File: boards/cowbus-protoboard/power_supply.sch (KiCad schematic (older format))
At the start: 3 parts

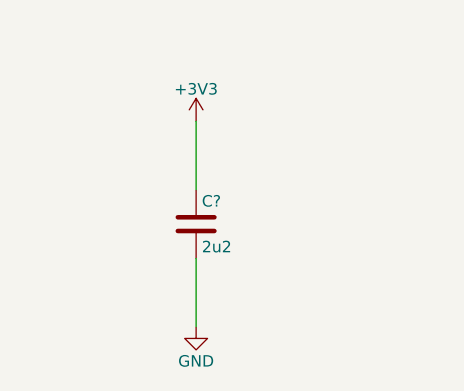
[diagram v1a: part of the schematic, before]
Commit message: values added, 100n for uC added
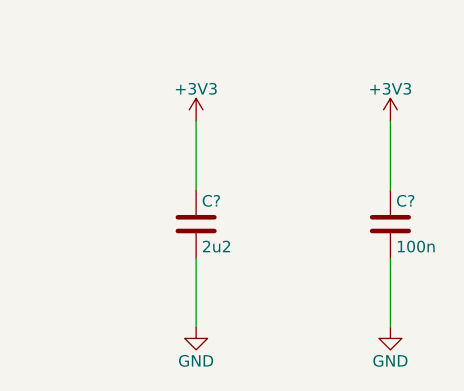
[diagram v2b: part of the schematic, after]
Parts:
- added C?: 100n, symbol C
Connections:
- net +3V3: now also C?.1
- net GND: now also C?.2
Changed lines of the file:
@@
 encoding utf-8
 Sheet 3 6
-Title ""
-Date ""
-Rev ""
+Title "cowbus protoboard"
+Date "2015-07-15"
+Rev "0.9"
 Comp ""
 Comment1 ""
@@
 Wire Wire Line
 	4450 3450 4450 4000
+$Comp
+L GND #PWR?
+U 1 1 55A95D68
+P 8250 4600
+F 0 "#PWR?" H 8250 4350 50  0001 C CNN
+F 1 "GND" H 8250 4450 50  0000 C CNN
+F 2 "" H 8250 4600 60  0000 C CNN
+F 3 "" H 8250 4600 60  0000 C CNN
+	1    8250 4600
+	1    0    0    -1
+$EndComp
+$Comp
+L +3V3 #PWR?
+U 1 1 55A95D6E
+P 8250 3700
+F 0 "#PWR?" H 8250 3550 50  0001 C CNN
+F 1 "+3V3" H 8250 3840 50  0000 C CNN
+F 2 "" H 8250 3700 60  0000 C CNN
+F 3 "" H 8250 3700 60  0000 C CNN
+	1    8250 3700
+	1    0    0    -1
+$EndComp
+$Comp
+L C C?
+U 1 1 55A95D76
+P 8250 4150
+F 0 "C?" H 8275 4250 50  0000 L CNN
+F 1 "100n" H 8275 4050 50  0000 L CNN
+F 2 "" H 8288 4000 30  0000 C CNN
+F 3 "" H 8250 4150 60  0000 C CNN
+	1    8250 4150
+	1    0    0    -1
+$EndComp
+Wire Wire Line
+	8250 4000 8250 3700
+Wire Wire Line
+	8250 4600 8250 4300
 $EndSCHEMATC

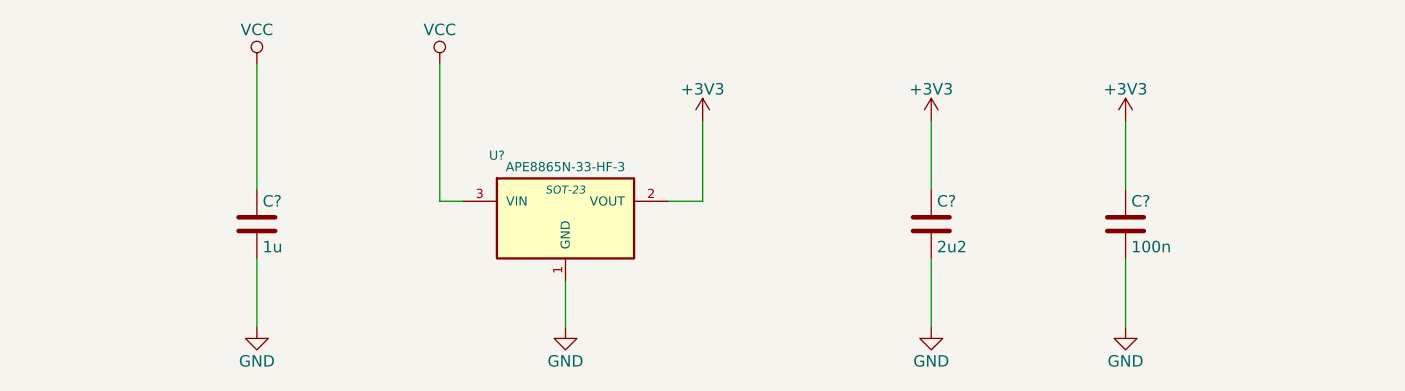
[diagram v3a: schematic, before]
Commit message: some footprint assignments done
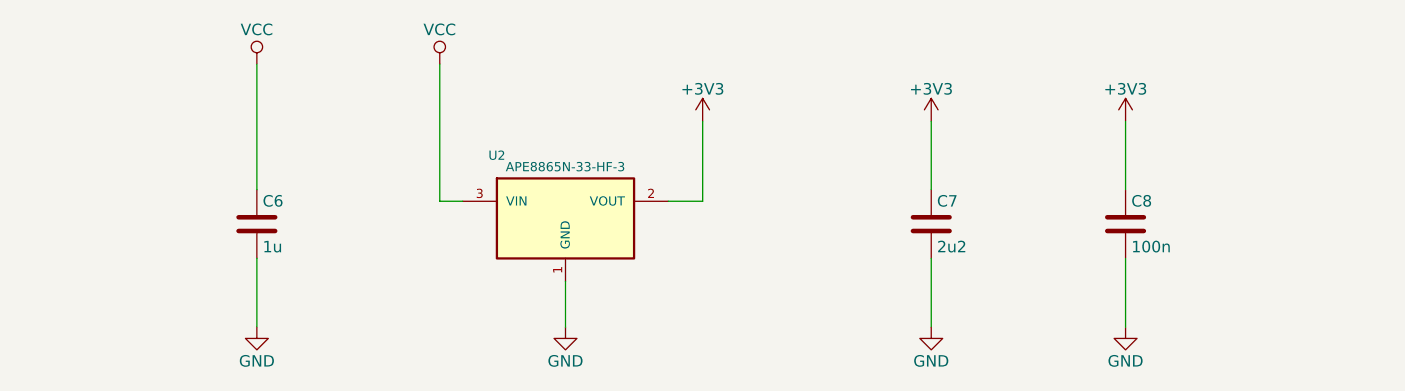
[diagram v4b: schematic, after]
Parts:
- C6, C7, C8: renamed from C?; footprint (none) -> Capacitors_SMD:C_0805_HandSoldering
- U2: renamed from U?; footprint SOT-23 -> (none)
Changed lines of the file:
@@
 $EndDescr
 $Comp
-L APE8865N-33-HF-3 U?
+L APE8865N-33-HF-3 U2
 U 1 1 55A5144A
 P 5800 4100
-F 0 "U?" H 5500 4350 40  0000 C CNN
+F 0 "U2" H 5500 4350 40  0000 C CNN
 F 1 "APE8865N-33-HF-3" H 5800 4300 40  0000 C CNN
-F 2 "SOT-23" H 5800 4200 35  0000 C CIN
+F 2 "" H 5800 4200 35  0001 C CIN
 F 3 "" H 5800 4100 60  0000 C CNN
 	1    5800 4100
@@
 $EndComp
 $Comp
-L C C?
+L C C6
 U 1 1 55A51451
 P 4450 4150
-F 0 "C?" H 4475 4250 50  0000 L CNN
+F 0 "C6" H 4475 4250 50  0000 L CNN
 F 1 "1u" H 4475 4050 50  0000 L CNN
-F 2 "" H 4488 4000 30  0000 C CNN
+F 2 "Capacitors_SMD:C_0805_HandSoldering" H 4488 4000 30  0001 C CNN
 F 3 "" H 4450 4150 60  0000 C CNN
 	1    4450 4150
@@
 $EndComp
 $Comp
-L C C?
+L C C7
 U 1 1 55A51458
 P 7400 4150
-F 0 "C?" H 7425 4250 50  0000 L CNN
+F 0 "C7" H 7425 4250 50  0000 L CNN
 F 1 "2u2" H 7425 4050 50  0000 L CNN
-F 2 "" H 7438 4000 30  0000 C CNN
+F 2 "Capacitors_SMD:C_0805_HandSoldering" H 7438 4000 30  0001 C CNN
 F 3 "" H 7400 4150 60  0000 C CNN
 	1    7400 4150
@@
 $EndComp
 $Comp
-L VCC #PWR?
+L VCC #PWR022
 U 1 1 55A515B6
 P 5250 3450
-F 0 "#PWR?" H 5250 3300 50  0001 C CNN
+F 0 "#PWR022" H 5250 3300 50  0001 C CNN
 F 1 "VCC" H 5250 3600 50  0000 C CNN
 F 2 "" H 5250 3450 60  0000 C CNN
@@
 	5250 3450 5250 4050
 $Comp
-L +3V3 #PWR?
+L +3V3 #PWR023
 U 1 1 55A515EF
 P 6400 3700
-F 0 "#PWR?" H 6400 3550 50  0001 C CNN
+F 0 "#PWR023" H 6400 3550 50  0001 C CNN
 F 1 "+3V3" H 6400 3840 50  0000 C CNN
 F 2 "" H 6400 3700 60  0000 C CNN
@@
 	6400 4050 6400 3700
 $Comp
-L GND #PWR?
+L GND #PWR024
 U 1 1 55A51658
 P 5800 4600
-F 0 "#PWR?" H 5800 4350 50  0001 C CNN
+F 0 "#PWR024" H 5800 4350 50  0001 C CNN
 F 1 "GND" H 5800 4450 50  0000 C CNN
 F 2 "" H 5800 4600 60  0000 C CNN
@@
 	5800 4600 5800 4400
 $Comp
-L VCC #PWR?
+L VCC #PWR025
 U 1 1 55A5185F
 P 4450 3450
-F 0 "#PWR?" H 4450 3300 50  0001 C CNN
+F 0 "#PWR025" H 4450 3300 50  0001 C CNN
 F 1 "VCC" H 4450 3600 50  0000 C CNN
 F 2 "" H 4450 3450 60  0000 C CNN
@@
 $EndComp
 $Comp
-L GND #PWR?
+L GND #PWR026
 U 1 1 55A51873
 P 4450 4600
-F 0 "#PWR?" H 4450 4350 50  0001 C CNN
+F 0 "#PWR026" H 4450 4350 50  0001 C CNN
 F 1 "GND" H 4450 4450 50  0000 C CNN
 F 2 "" H 4450 4600 60  0000 C CNN
@@
 $EndComp
 $Comp
-L GND #PWR?
+L GND #PWR027
 U 1 1 55A51887
 P 7400 4600
-F 0 "#PWR?" H 7400 4350 50  0001 C CNN
+F 0 "#PWR027" H 7400 4350 50  0001 C CNN
 F 1 "GND" H 7400 4450 50  0000 C CNN
 F 2 "" H 7400 4600 60  0000 C CNN
@@
 $EndComp
 $Comp
-L +3V3 #PWR?
+L +3V3 #PWR028
 U 1 1 55A518AE
 P 7400 3700
-F 0 "#PWR?" H 7400 3550 50  0001 C CNN
+F 0 "#PWR028" H 7400 3550 50  0001 C CNN
 F 1 "+3V3" H 7400 3840 50  0000 C CNN
 F 2 "" H 7400 3700 60  0000 C CNN
@@
 	4450 3450 4450 4000
 $Comp
-L GND #PWR?
+L GND #PWR029
 U 1 1 55A95D68
 P 8250 4600
-F 0 "#PWR?" H 8250 4350 50  0001 C CNN
+F 0 "#PWR029" H 8250 4350 50  0001 C CNN
 F 1 "GND" H 8250 4450 50  0000 C CNN
 F 2 "" H 8250 4600 60  0000 C CNN
@@
 $EndComp
 $Comp
-L +3V3 #PWR?
+L +3V3 #PWR030
 U 1 1 55A95D6E
 P 8250 3700
-F 0 "#PWR?" H 8250 3550 50  0001 C CNN
+F 0 "#PWR030" H 8250 3550 50  0001 C CNN
 F 1 "+3V3" H 8250 3840 50  0000 C CNN
 F 2 "" H 8250 3700 60  0000 C CNN
@@
 $EndComp
 $Comp
-L C C?
+L C C8
 U 1 1 55A95D76
 P 8250 4150
-F 0 "C?" H 8275 4250 50  0000 L CNN
+F 0 "C8" H 8275 4250 50  0000 L CNN
 F 1 "100n" H 8275 4050 50  0000 L CNN
-F 2 "" H 8288 4000 30  0000 C CNN
+F 2 "Capacitors_SMD:C_0805_HandSoldering" H 8288 4000 30  0001 C CNN
 F 3 "" H 8250 4150 60  0000 C CNN
 	1    8250 4150

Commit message: first version of layout for protoboard
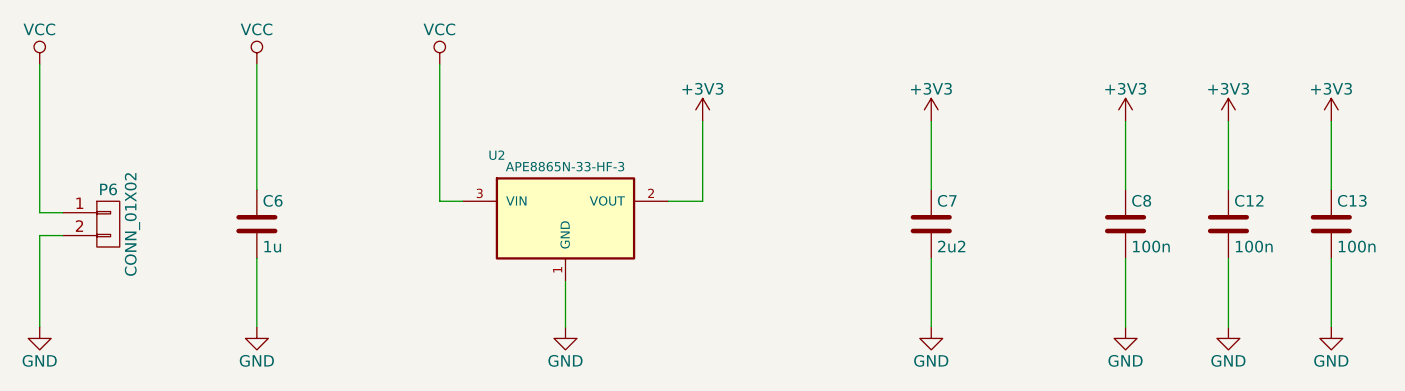
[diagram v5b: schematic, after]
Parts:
- added C12, C13: 100n, Capacitors_SMD:C_0805_HandSoldering, symbol C
- added P6: CONN_01X02, Pin_Headers:Pin_Header_Straight_1x02, symbol CONN_01X02
- U2: footprint (none) -> Housings_SOT-23_SOT-143_TSOT-6:SOT-23_Handsoldering
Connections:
- net +3V3: now also C12.1, C13.1
- net GND: now also C12.2, C13.2, P6.2 (P2)
- net VCC: now also P6.1 (P1)
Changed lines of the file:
@@
 EESchema Schematic File Version 2
+LIBS:cowbus-protoboard-rescue
 LIBS:power
 LIBS:device
@@
 LIBS:nrf24l01plus-module
 LIBS:i2c
+LIBS:led_rgb_reichelt
 LIBS:cowbus-protoboard-cache
 EELAYER 25 0
@@
 F 0 "U2" H 5500 4350 40  0000 C CNN
 F 1 "APE8865N-33-HF-3" H 5800 4300 40  0000 C CNN
-F 2 "" H 5800 4200 35  0001 C CIN
+F 2 "Housings_SOT-23_SOT-143_TSOT-6:SOT-23_Handsoldering" H 5800 4200 35  0001 C CIN
 F 3 "" H 5800 4100 60  0000 C CNN
 	1    5800 4100
@@
 $EndComp
 $Comp
-L VCC #PWR022
+L VCC #PWR27
 U 1 1 55A515B6
 P 5250 3450
-F 0 "#PWR022" H 5250 3300 50  0001 C CNN
+F 0 "#PWR27" H 5250 3300 50  0001 C CNN
 F 1 "VCC" H 5250 3600 50  0000 C CNN
 F 2 "" H 5250 3450 60  0000 C CNN
@@
 	5250 3450 5250 4050
 $Comp
-L +3V3 #PWR023
+L +3V3 #PWR29
 U 1 1 55A515EF
 P 6400 3700
-F 0 "#PWR023" H 6400 3550 50  0001 C CNN
+F 0 "#PWR29" H 6400 3550 50  0001 C CNN
 F 1 "+3V3" H 6400 3840 50  0000 C CNN
 F 2 "" H 6400 3700 60  0000 C CNN
@@
 	6400 4050 6400 3700
 $Comp
-L GND #PWR024
+L GND #PWR28
 U 1 1 55A51658
 P 5800 4600
-F 0 "#PWR024" H 5800 4350 50  0001 C CNN
+F 0 "#PWR28" H 5800 4350 50  0001 C CNN
 F 1 "GND" H 5800 4450 50  0000 C CNN
 F 2 "" H 5800 4600 60  0000 C CNN
@@
 	5800 4600 5800 4400
 $Comp
-L VCC #PWR025
+L VCC #PWR25
 U 1 1 55A5185F
 P 4450 3450
-F 0 "#PWR025" H 4450 3300 50  0001 C CNN
+F 0 "#PWR25" H 4450 3300 50  0001 C CNN
 F 1 "VCC" H 4450 3600 50  0000 C CNN
 F 2 "" H 4450 3450 60  0000 C CNN
@@
 $EndComp
 $Comp
-L GND #PWR026
+L GND #PWR26
 U 1 1 55A51873
 P 4450 4600
-F 0 "#PWR026" H 4450 4350 50  0001 C CNN
+F 0 "#PWR26" H 4450 4350 50  0001 C CNN
 F 1 "GND" H 4450 4450 50  0000 C CNN
 F 2 "" H 4450 4600 60  0000 C CNN
@@
 $EndComp
 $Comp
-L GND #PWR027
+L GND #PWR31
 U 1 1 55A51887
 P 7400 4600
-F 0 "#PWR027" H 7400 4350 50  0001 C CNN
+F 0 "#PWR31" H 7400 4350 50  0001 C CNN
 F 1 "GND" H 7400 4450 50  0000 C CNN
 F 2 "" H 7400 4600 60  0000 C CNN
@@
 $EndComp
 $Comp
-L +3V3 #PWR028
+L +3V3 #PWR30
 U 1 1 55A518AE
 P 7400 3700
-F 0 "#PWR028" H 7400 3550 50  0001 C CNN
+F 0 "#PWR30" H 7400 3550 50  0001 C CNN
 F 1 "+3V3" H 7400 3840 50  0000 C CNN
 F 2 "" H 7400 3700 60  0000 C CNN
@@
 	4450 3450 4450 4000
 $Comp
-L GND #PWR029
+L GND #PWR33
 U 1 1 55A95D68
 P 8250 4600
-F 0 "#PWR029" H 8250 4350 50  0001 C CNN
+F 0 "#PWR33" H 8250 4350 50  0001 C CNN
 F 1 "GND" H 8250 4450 50  0000 C CNN
 F 2 "" H 8250 4600 60  0000 C CNN
@@
 $EndComp
 $Comp
-L +3V3 #PWR030
+L +3V3 #PWR32
 U 1 1 55A95D6E
 P 8250 3700
-F 0 "#PWR030" H 8250 3550 50  0001 C CNN
+F 0 "#PWR32" H 8250 3550 50  0001 C CNN
 F 1 "+3V3" H 8250 3840 50  0000 C CNN
 F 2 "" H 8250 3700 60  0000 C CNN
@@
 Wire Wire Line
 	8250 4600 8250 4300
+$Comp
+L CONN_01X02 P6
+U 1 1 55BA81F9
+P 3800 4150
+F 0 "P6" H 3800 4300 50  0000 C CNN
+F 1 "CONN_01X02" V 3900 4150 50  0000 C CNN
+F 2 "Pin_Headers:Pin_Header_Straight_1x02" H 3800 4150 60  0001 C CNN
+F 3 "" H 3800 4150 60  0000 C CNN
+	1    3800 4150
+	1    0    0    -1
+$EndComp
+$Comp
+L VCC #PWR23
+U 1 1 55BA82A3
+P 3500 3450
+F 0 "#PWR23" H 3500 3300 50  0001 C CNN
+F 1 "VCC" H 3500 3600 50  0000 C CNN
+F 2 "" H 3500 3450 60  0000 C CNN
+F 3 "" H 3500 3450 60  0000 C CNN
+	1    3500 3450
+	1    0    0    -1
+$EndComp
+Wire Wire Line
+	3500 3450 3500 4100
+$Comp
+L GND #PWR24
+U 1 1 55BA82C3
+P 3500 4600
+F 0 "#PWR24" H 3500 4350 50  0001 C CNN
+F 1 "GND" H 3500 4450 50  0000 C CNN
+F 2 "" H 3500 4600 60  0000 C CNN
+F 3 "" H 3500 4600 60  0000 C CNN
+	1    3500 4600
+	1    0    0    -1
+$EndComp
+Wire Wire Line
+	3500 4200 3500 4600
+Wire Wire Line
+	3600 4200 3500 4200
+Wire Wire Line
+	3500 4100 3600 4100
+$Comp
+L GND #PWR35
+U 1 1 55BBC2D8
+P 8700 4600
+F 0 "#PWR35" H 8700 4350 50  0001 C CNN
+F 1 "GND" H 8700 4450 50  0000 C CNN
+F 2 "" H 8700 4600 60  0000 C CNN
+F 3 "" H 8700 4600 60  0000 C CNN
+	1    8700 4600
+	1    0    0    -1
+$EndComp
+$Comp
+L +3V3 #PWR34
+U 1 1 55BBC2DE
+P 8700 3700
+F 0 "#PWR34" H 8700 3550 50  0001 C CNN
+F 1 "+3V3" H 8700 3840 50  0000 C CNN
+F 2 "" H 8700 3700 60  0000 C CNN
+F 3 "" H 8700 3700 60  0000 C CNN
+	1    8700 3700
+	1    0    0    -1
+$EndComp
+$Comp
+L C C12
+U 1 1 55BBC2E4
+P 8700 4150
+F 0 "C12" H 8725 4250 50  0000 L CNN
+F 1 "100n" H 8725 4050 50  0000 L CNN
+F 2 "Capacitors_SMD:C_0805_HandSoldering" H 8738 4000 30  0001 C CNN
+F 3 "" H 8700 4150 60  0000 C CNN
+	1    8700 4150
+	1    0    0    -1
+$EndComp
+Wire Wire Line
+	8700 4000 8700 3700
+Wire Wire Line
+	8700 4600 8700 4300
+$Comp
+L GND #PWR37
+U 1 1 55BBC31A
+P 9150 4600
+F 0 "#PWR37" H 9150 4350 50  0001 C CNN
+F 1 "GND" H 9150 4450 50  0000 C CNN
+F 2 "" H 9150 4600 60  0000 C CNN
+F 3 "" H 9150 4600 60  0000 C CNN
+	1    9150 4600
+	1    0    0    -1
+$EndComp
+$Comp
+L +3V3 #PWR36
+U 1 1 55BBC320
+P 9150 3700
+F 0 "#PWR36" H 9150 3550 50  0001 C CNN
+F 1 "+3V3" H 9150 3840 50  0000 C CNN
+F 2 "" H 9150 3700 60  0000 C CNN
+F 3 "" H 9150 3700 60  0000 C CNN
+	1    9150 3700
+	1    0    0    -1
+$EndComp
+$Comp
+L C C13
+U 1 1 55BBC326
+P 9150 4150
+F 0 "C13" H 9175 4250 50  0000 L CNN
+F 1 "100n" H 9175 4050 50  0000 L CNN
+F 2 "Capacitors_SMD:C_0805_HandSoldering" H 9188 4000 30  0001 C CNN
+F 3 "" H 9150 4150 60  0000 C CNN
+	1    9150 4150
+	1    0    0    -1
+$EndComp
+Wire Wire Line
+	9150 4000 9150 3700
+Wire Wire Line
+	9150 4600 9150 4300
 $EndSCHEMATC

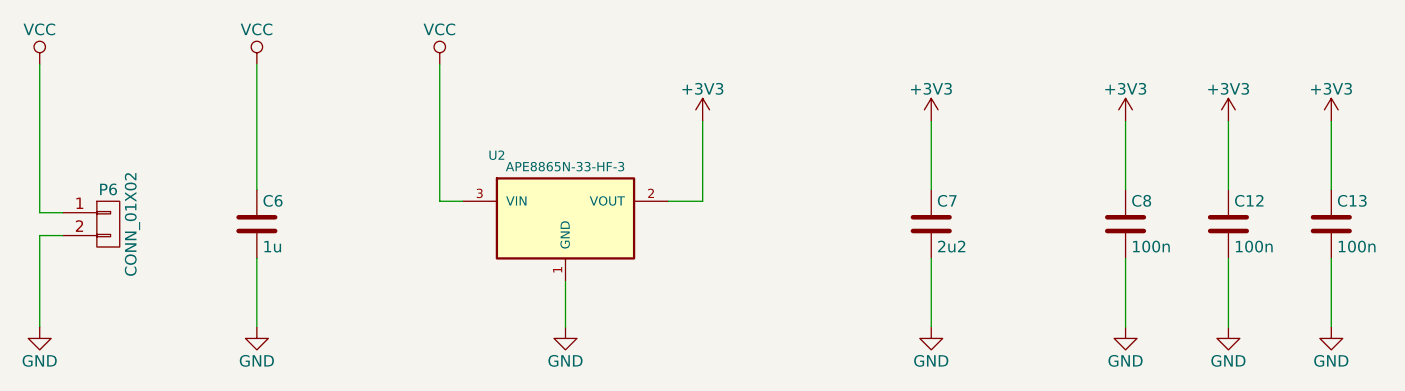
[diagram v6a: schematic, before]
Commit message: wrong LDO pinout corrected + README
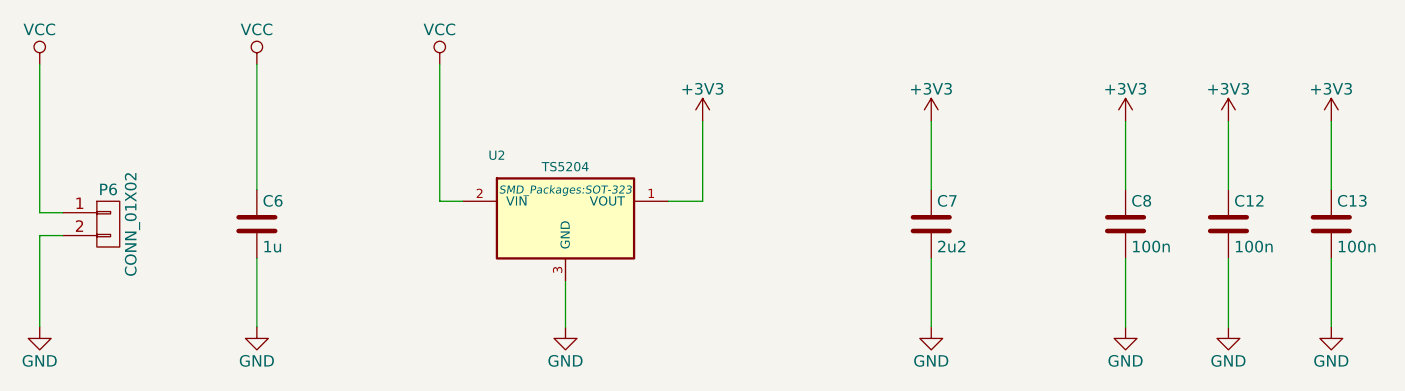
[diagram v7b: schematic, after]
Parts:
- removed U2: APE8865N-33-HF-3, Housings_SOT-23_SOT-143_TSOT-6:SOT-23_Handsoldering, symbol APE8865N-33-HF-3
- added U2: TS5204, SMD_Packages:SOT-323, symbol TS5204
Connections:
- net +3V3: now also U2.1 (VOUT)
- net GND: now also U2.3 (GND)
- net VCC: now also U2.2 (VIN)
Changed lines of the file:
@@
 LIBS:i2c
 LIBS:led_rgb_reichelt
+LIBS:ts5204
 LIBS:cowbus-protoboard-cache
 EELAYER 25 0
@@
 $EndDescr
 $Comp
-L APE8865N-33-HF-3 U2
-U 1 1 55A5144A
-P 5800 4100
-F 0 "U2" H 5500 4350 40  0000 C CNN
-F 1 "APE8865N-33-HF-3" H 5800 4300 40  0000 C CNN
-F 2 "Housings_SOT-23_SOT-143_TSOT-6:SOT-23_Handsoldering" H 5800 4200 35  0001 C CIN
-F 3 "" H 5800 4100 60  0000 C CNN
-	1    5800 4100
-	1    0    0    -1
-$EndComp
-$Comp
 L C C6
 U 1 1 55A51451
@@
 Wire Wire Line
 	9150 4600 9150 4300
+$Comp
+L TS5204 U2
+U 1 1 55BCF895
+P 5800 4100
+F 0 "U2" H 5500 4350 40  0000 C CNN
+F 1 "TS5204" H 5800 4300 40  0000 C CNN
+F 2 "SMD_Packages:SOT-323" H 5800 4200 35  0000 C CIN
+F 3 "" H 5800 4100 60  0000 C CNN
+	1    5800 4100
+	1    0    0    -1
+$EndComp
 $EndSCHEMATC

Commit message: added schematics rev, annotation fixed, OSHW logo
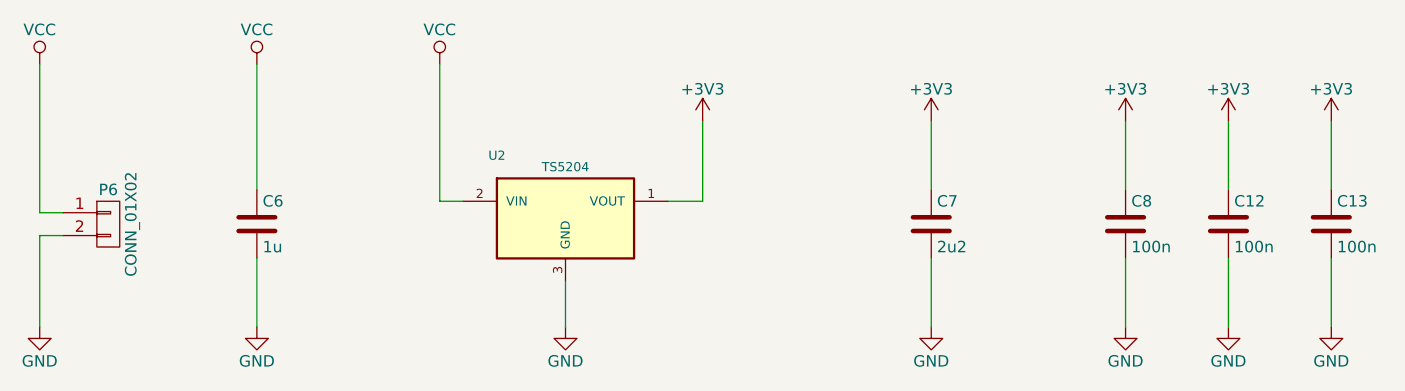
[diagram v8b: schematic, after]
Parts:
- U2: footprint SMD_Packages:SOT-323 -> Housings_SOT-23_SOT-143_TSOT-6:SOT-23_Handsoldering
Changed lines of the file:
@@
 Title "cowbus protoboard"
 Date "2015-07-15"
-Rev "0.9"
+Rev "1"
 Comp ""
 Comment1 ""
@@
 F 0 "U2" H 5500 4350 40  0000 C CNN
 F 1 "TS5204" H 5800 4300 40  0000 C CNN
-F 2 "SMD_Packages:SOT-323" H 5800 4200 35  0000 C CIN
+F 2 "Housings_SOT-23_SOT-143_TSOT-6:SOT-23_Handsoldering" H 5800 4200 35  0001 C CIN
 F 3 "" H 5800 4100 60  0000 C CNN
 	1    5800 4100
